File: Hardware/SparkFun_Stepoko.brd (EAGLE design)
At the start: 150 x 82 mm, 179 parts, among them J1 AVR ISP, Q1 16MHZ, Q2 100A/100V, U1 ATMEGA328, U2 CY7C65213, U3 74LVC1G04, U4 LM25011, U5 DRV8811, U6 74HC7014D, U7 74AHC1G08, U8 DRV8811, U9 DRV8811

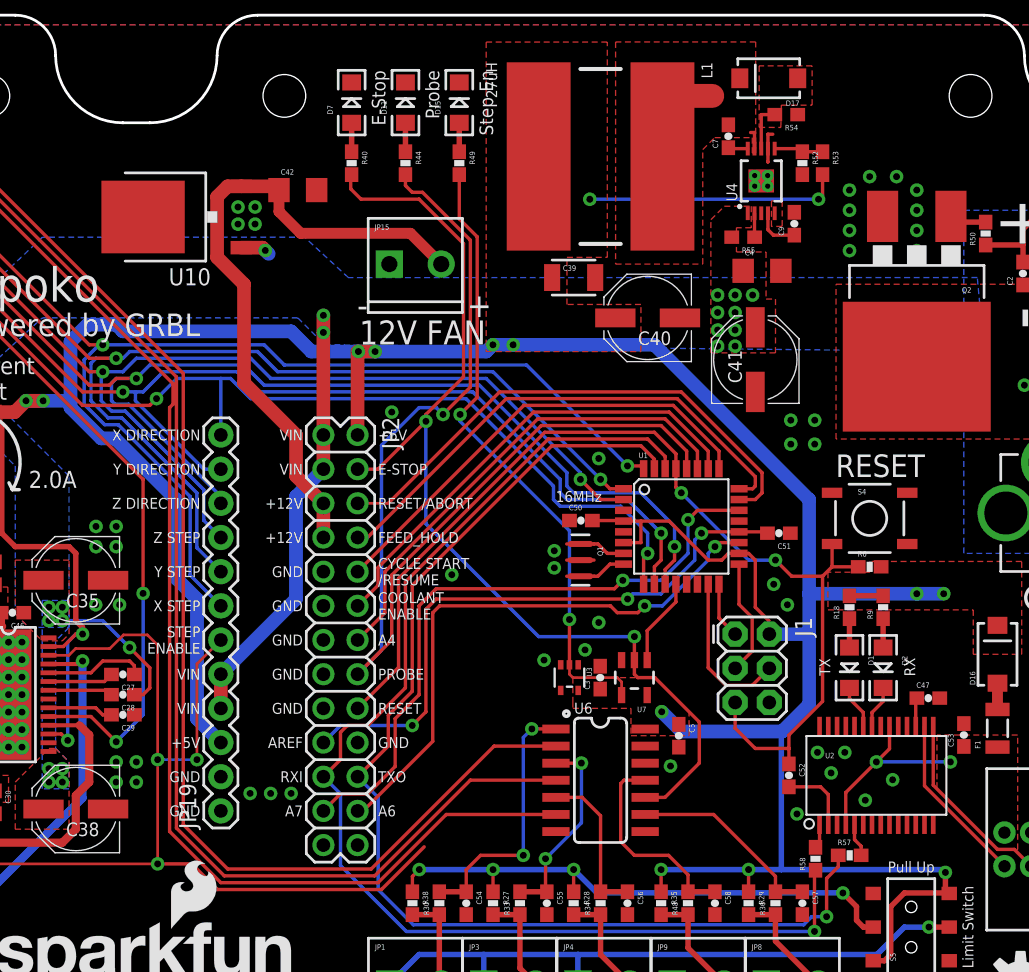
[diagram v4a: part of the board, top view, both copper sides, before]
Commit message: finished modifications from proto review
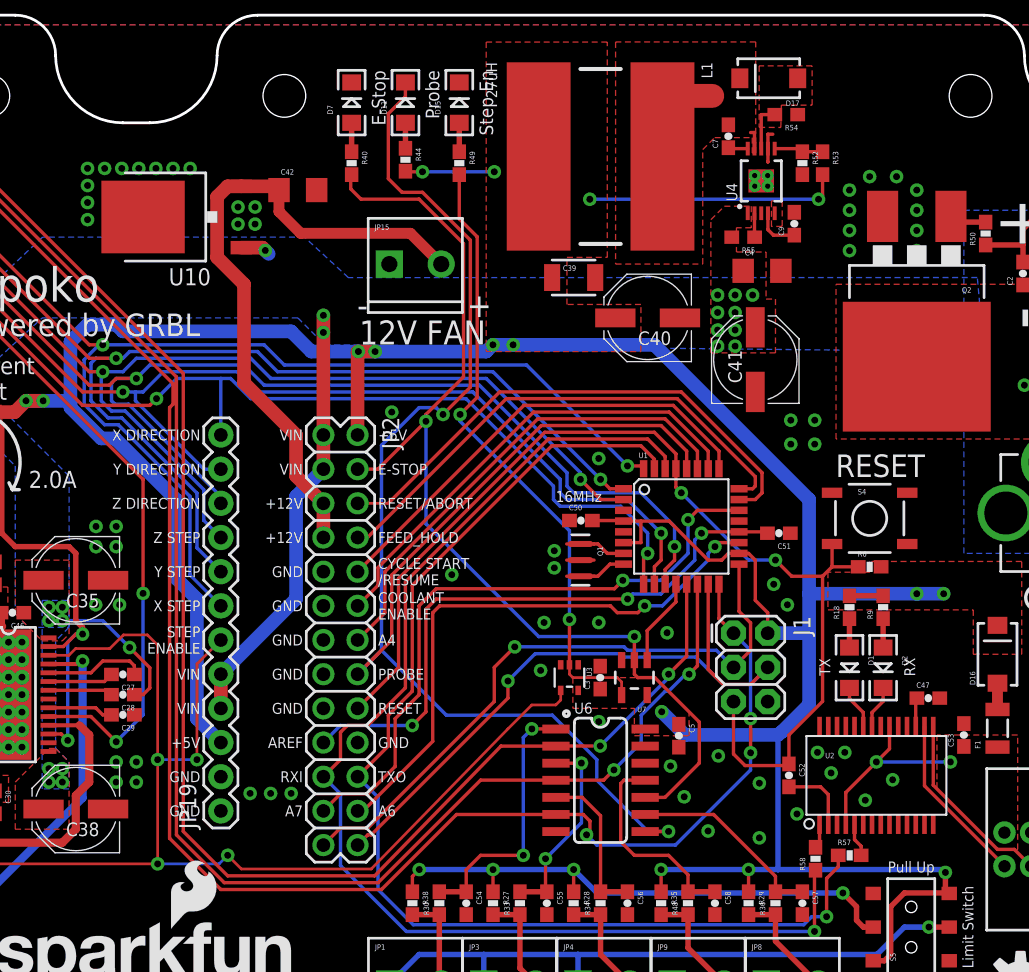
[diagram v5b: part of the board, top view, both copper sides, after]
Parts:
- moved R44 0.25 mm to (95.0, 71.3)
- moved J1 0.14 mm to (119.4, 36.1)
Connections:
- net 5V: now also R44.2
- net A5-PROBE: now also D11.C; no longer R44.2
- net GND: no longer D11.C
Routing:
- net SCK-D13-SPINDLE_DIR: track 8.67 -> 47.3 mm, vias 0 -> 1
- net MOSI-D11-SPINDLE_PWM: track 11.8 -> 50.3 mm, vias 0 -> 1
- net A5-PROBE: track 81.8 -> 119.7 mm, vias 1 -> 2
- net MISO-D12-LIMIT-Z: track 97.8 -> 127.8 mm, vias 0 -> 3
- net D10-LIM-Y: track 114.0 -> 136.0 mm, vias 0 -> 2
- net D9-LIM-X: track 128.4 -> 147.1 mm, vias 0 -> 2
- net STEP_ENABLE: track 150.4 -> 165.1 mm, vias 8 -> 9
- net 5V: track 463.4 -> 470.3 mm, vias 26 -> 28
- net RESET: track 79.0 -> 80.9 mm
- net GND: vias 108 -> 125

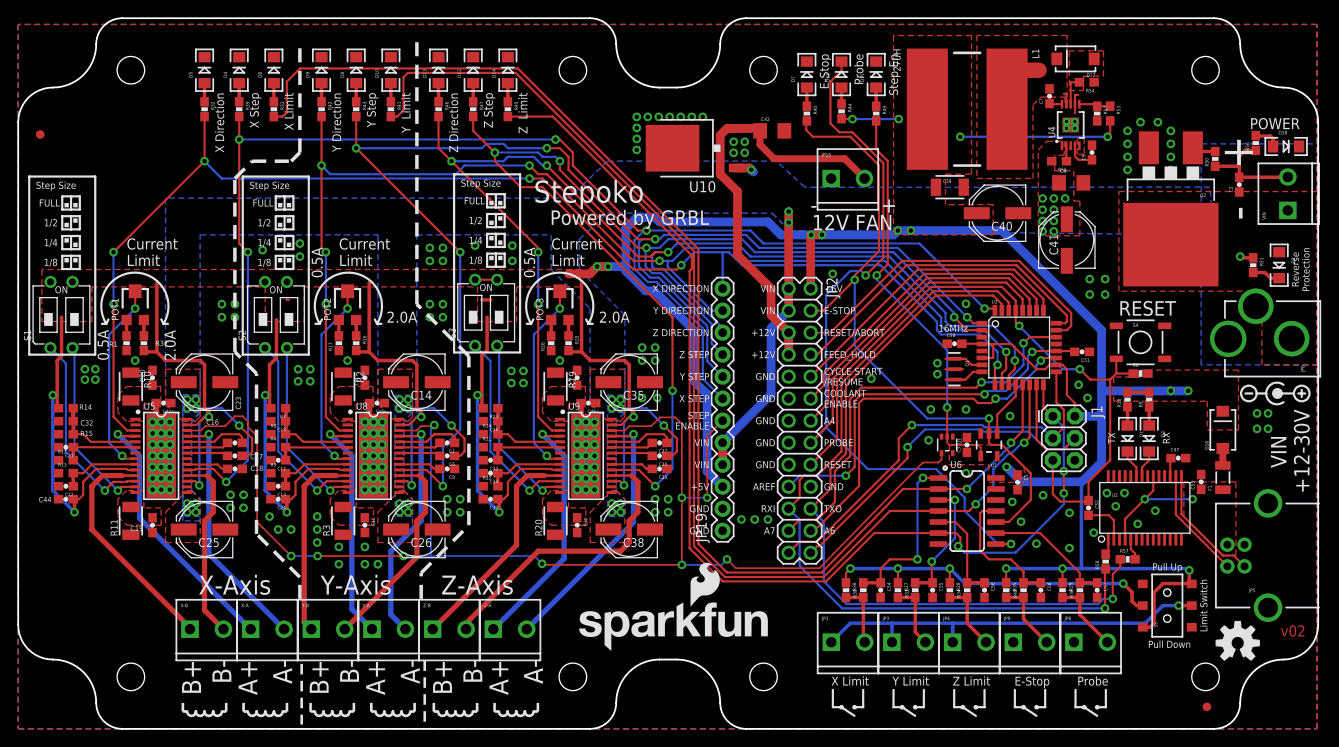
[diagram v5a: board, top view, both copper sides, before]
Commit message: made changes and added logos. Added test points
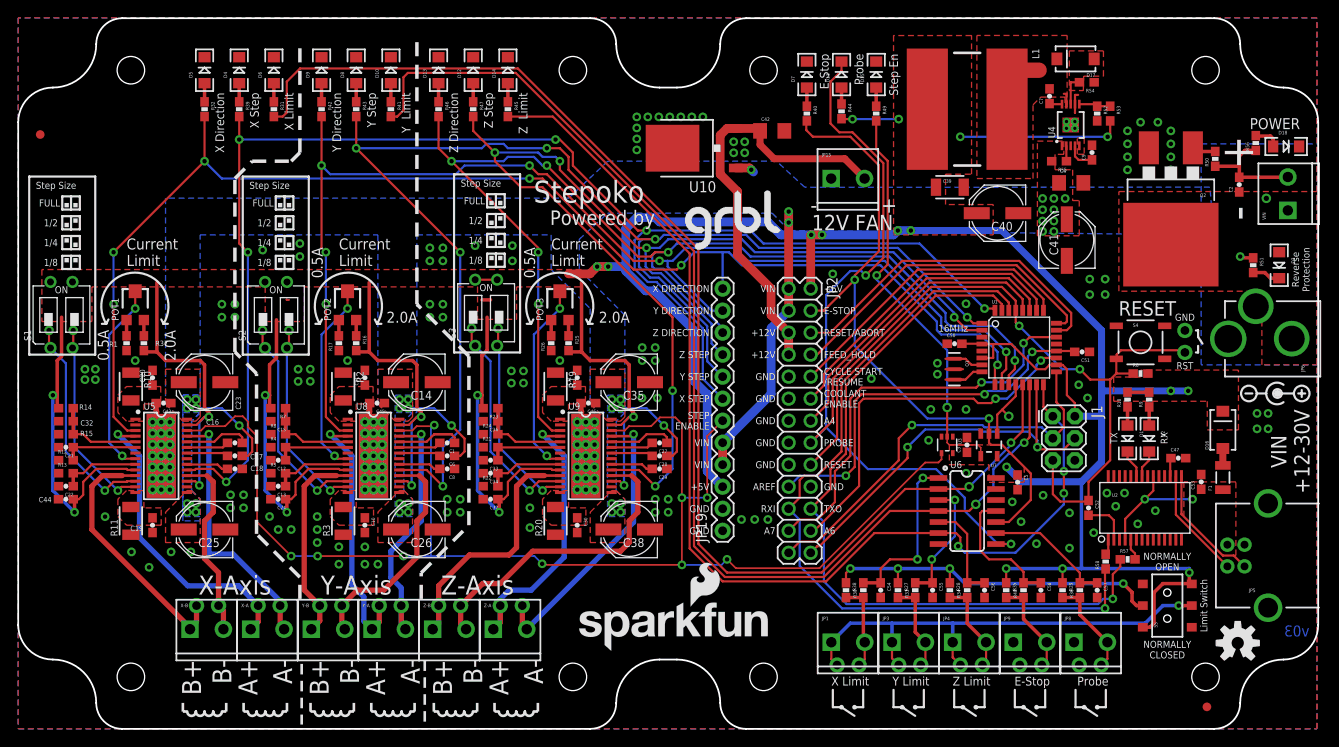
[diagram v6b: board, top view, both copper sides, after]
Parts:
- added LOGO3: SFE_LOGO_NAME_FLAME.2_INCH, SparkFun-Aesthetics:SFE_LOGO_NAME_FLAME_.2
- JP19: value M12PTH -> (none)
- JP2: value M13X22X13 -> (none)
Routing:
- net N$4: track 47.7 -> 56.6 mm, vias 1 -> 4
- net RESET: track 80.9 -> 89.7 mm, vias 2 -> 3
- net N$89: track 29.0 -> 33.6 mm, vias 1 -> 2
- net N$71: track 31.0 -> 35.1 mm, vias 1 -> 2
- net MOSI-D11-SPINDLE_PWM: track 50.3 -> 46.3 mm, vias 1 -> 2
- net N$56: track 26.6 -> 29.7 mm, vias 1 -> 2
- net N$90: track 30.2 -> 33.2 mm, vias 1 -> 2
- net N$53: track 8.53 -> 11.5 mm, vias 0 -> 1
- net N$58: track 27.3 -> 30.2 mm, vias 1 -> 2
- net N$7: track 7.22 -> 10.1 mm, vias 0 -> 1
- net N$57: track 8.32 -> 11.2 mm, vias 0 -> 1
- net N$37: track 26.7 -> 29.6 mm, vias 0 -> 1
- net N$42: track 7.63 -> 10.5 mm, vias 0 -> 1
- net N$43: track 8.11 -> 10.9 mm, vias 0 -> 1
- net N$87: track 26.0 -> 28.7 mm, vias 0 -> 1
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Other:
- board text added: "ARDUINO MAP"
- board text added: "D0- RX D1- TX D2- STEP X D3- STEP Y D4- STEP Z D5- DIR X D6- DIR Y D7- DIR Z D8- STEP EN D9- LIM X D10- LIM Y D11- SPIN PWM D12- LIM Z D13- SPIN DIR A0- RESET/ABORT A1- FEED HOLD A2- CYCLE START A3- COOLANT EN A4- UNUSED A5- PROBE A6- UNUSED A7- UNUSED"
- board text added: "NORMALLY CLOSED"
- board text added: "NORMALLY OPEN"
- board text added: "Powered by"
- board text added: "RST"
- board text added: "v03"
- board text removed: "Powered by GRBL"
- board text removed: "Pull Down"
- board text removed: "Pull Up"
- board text removed: "v02"

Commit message: made changes from issues in repo
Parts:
- U7: device SparkFun-DigitalIC:SOT23-5 -> SparkFun-DigitalIC:SOT353

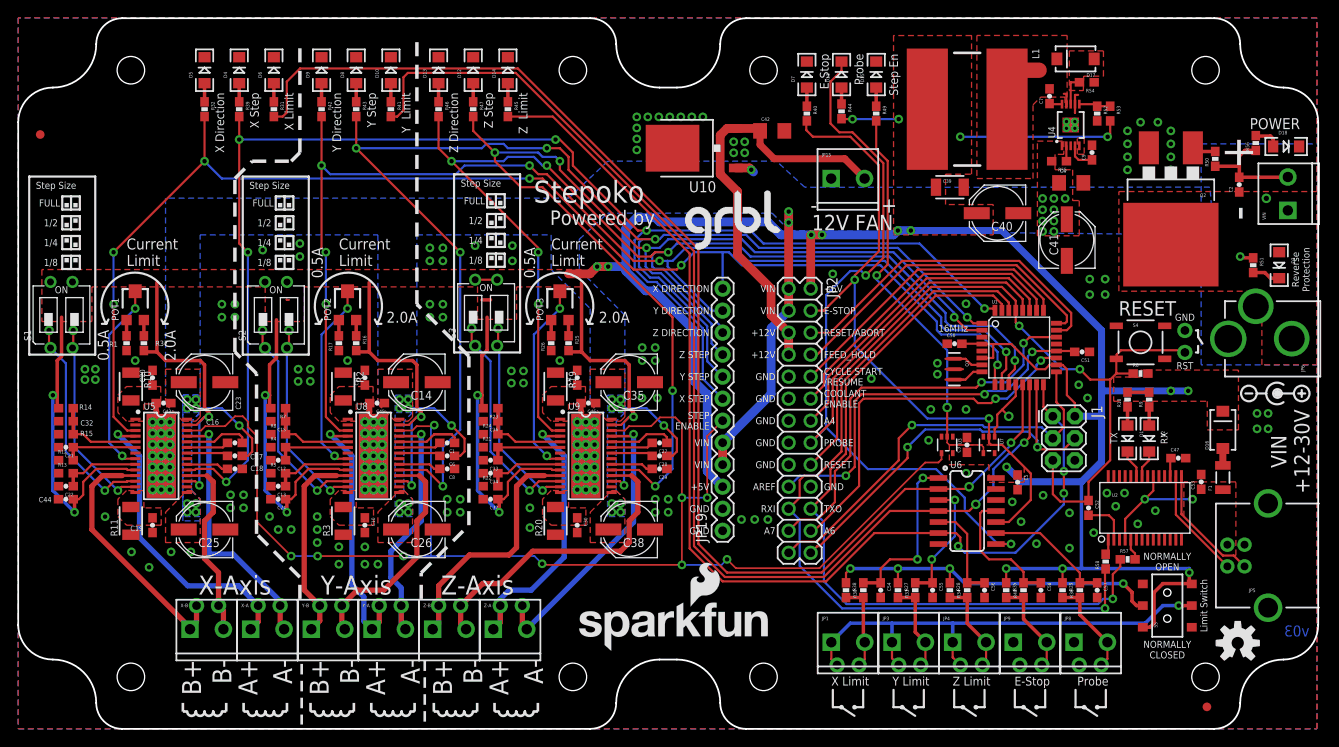
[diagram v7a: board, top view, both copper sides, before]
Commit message: fixing high impedance issues
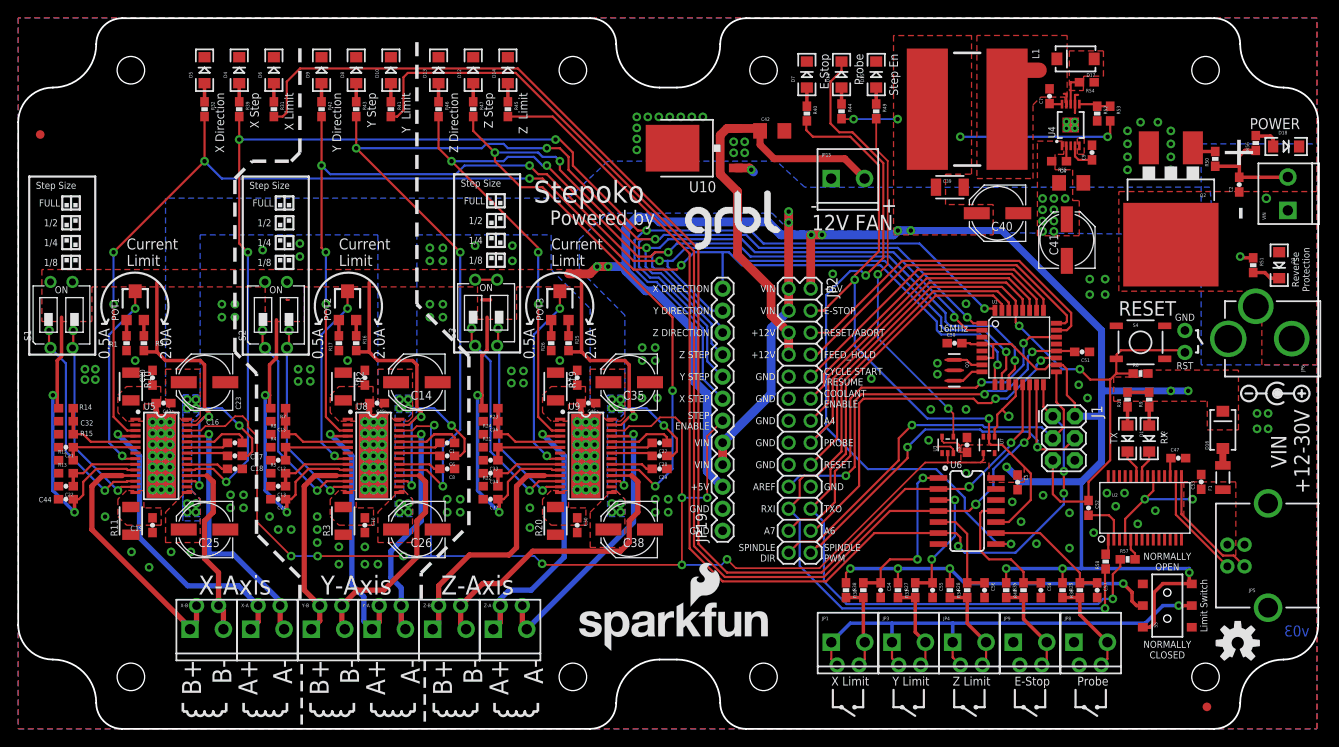
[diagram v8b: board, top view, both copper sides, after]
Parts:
- LOGO2: device SparkFun-Aesthetics:SFE_LOGO_NAME_FLAME_.2 -> SparkFun-Aesthetics:SFE_LOGO_NAME_FLAME_.2@1
- U7: value 74AHC1G08 -> 7432SE
- moved R49 0.25 mm to (99.0, 71.3)
- moved Q1 0.13 mm to (108.0, 41.4)
- moved C50 0.06 mm to (108.0, 44.5)
- moved U3 0.06 mm to (107.3, 32.8), turned to 0 degrees
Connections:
- removed net STEP_EN_LOGIC: R49.2, U3.2, U7.4
- new net STEP-EN_LED: R49.2, U3.4
- net STEP_ENABLE: now also U3.2, U7.4; no longer U3.4
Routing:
- net STEP_EN_LOGIC: track 46.7 -> 0.00 mm, vias 2 -> 0
- net STEP-EN_LED: track 0.00 -> 41.3 mm, vias 0 -> 2
- net STEP_ENABLE: track 165.1 -> 171.0 mm
- net 5V: track 470.0 -> 474.1 mm
- net GND: track 5.83 -> 8.32 mm, vias 134 -> 131
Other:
- board text added: "SPINDLE DIR"
- board text added: "SPINDLE PWM"
